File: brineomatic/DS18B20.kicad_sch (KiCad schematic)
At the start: 4 parts

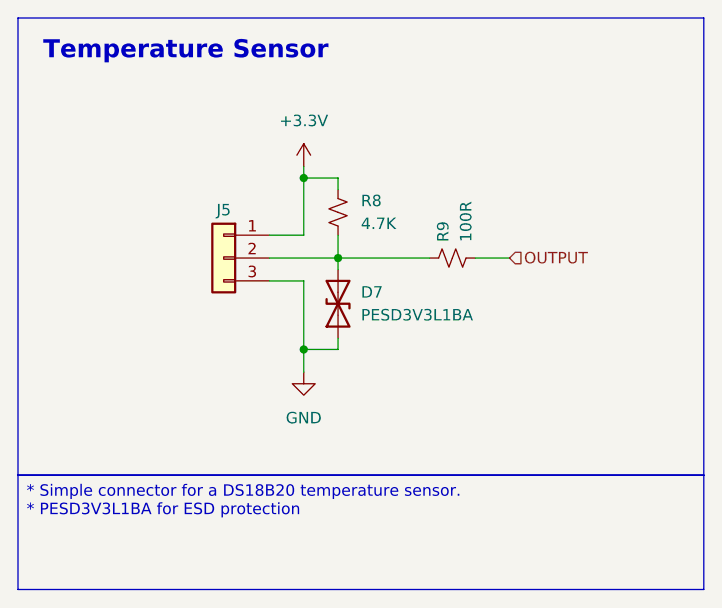
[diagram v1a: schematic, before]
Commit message: cleaned up hierarchical pin settings
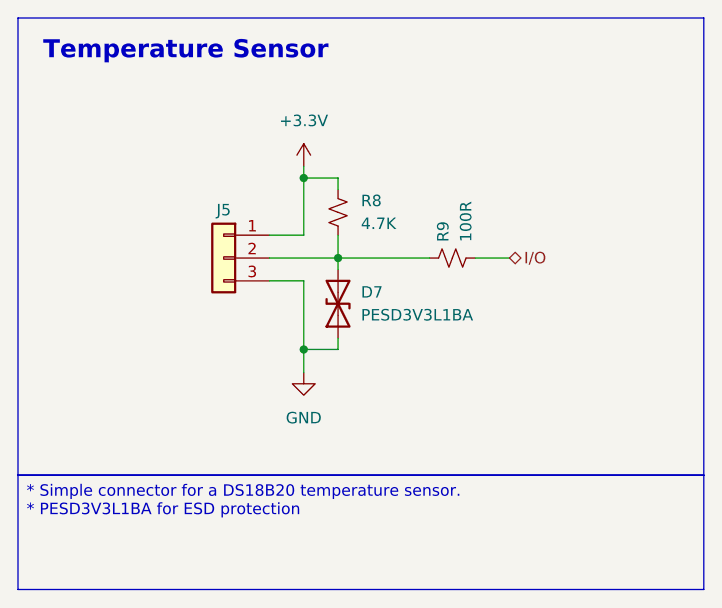
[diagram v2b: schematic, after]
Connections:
- net OUTPUT renamed I/O
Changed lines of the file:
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@@
 		)
 	)
-	(hierarchical_label "OUTPUT"
-		(shape input)
+	(hierarchical_label "I{slash}O"
+		(shape bidirectional)
 		(at 142.24 93.98 0)
 		(effects

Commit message: holy re-routing batman. board is fully routed first pass.
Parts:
- added C4: 1uF, Capacitor_SMD:C_0603_1608Metric, symbol Device:C_Small
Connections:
- net +3.3V: now also C4.1
- net GND: now also C4.2
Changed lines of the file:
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@@
+	(wire
+		(pts
+			(xy 119.38 104.14) (xy 97.79 104.14)
+		)
+		(stroke
+			(width 0)
+			(type default)
+		)
+	)
 	(wire
 		(pts
@@
 	(wire
 		(pts
+			(xy 119.38 85.09) (xy 97.79 85.09)
+		)
+		(stroke
+			(width 0)
+			(type default)
+		)
+	)
+	(wire
+		(pts
 			(xy 119.38 104.14) (xy 119.38 106.68)
 		)
@@
 	(wire
 		(pts
+			(xy 97.79 85.09) (xy 97.79 91.44)
+		)
+		(stroke
+			(width 0)
+			(type default)
+		)
+	)
+	(wire
+		(pts
 			(xy 123.19 91.44) (xy 123.19 93.98)
 		)
@@
 		(pts
 			(xy 123.19 104.14) (xy 123.19 102.87)
+		)
+		(stroke
+			(width 0)
+			(type default)
+		)
+	)
+	(wire
+		(pts
+			(xy 97.79 96.52) (xy 97.79 104.14)
 		)
 		(stroke
@@
 			)
 			(justify left)
+		)
+	)
+	(symbol
+		(lib_id "Device:C_Small")
+		(at 97.79 93.98 0)
+		(unit 1)
+		(exclude_from_sim no)
+		(in_bom yes)
+		(on_board yes)
+		(dnp no)
+		(fields_autoplaced yes)
+		(property "Reference" "C4"
+			(at 100.33 92.7162 0)
+			(effects
+				(font
+					(size 1.27 1.27)
+				)
+				(justify left)
+			)
+		)
+		(property "Value" "1uF"
+			(at 100.33 95.2562 0)
+			(effects
+				(font
+					(size 1.27 1.27)
+				)
+				(justify left)
+			)
+		)
+		(property "Footprint" "Capacitor_SMD:C_0603_1608Metric"
+			(at 97.79 93.98 0)
+			(effects
+				(font
+					(size 1.27 1.27)
+				)
+				(hide yes)
+			)
+		)
+		(property "Datasheet" "~"
+			(at 97.79 93.98 0)
+			(effects
+				(font
+					(size 1.27 1.27)
+				)
+				(hide yes)
+			)
+		)
+		(property "Description" ""
+			(at 97.79 93.98 0)
+			(effects
+				(font
+					(size 1.27 1.27)
+				)
+			)
+		)
+		(property "LCSC Part Name" ""
+			(at 97.79 93.98 0)
+			(effects
+				(font
+					(size 1.27 1.27)
+				)
+				(hide yes)
+			)
+		)
+		(property "Manufacturer" ""
+			(at 97.79 93.98 0)
+			(effects
+				(font
+					(size 1.27 1.27)
+				)
+				(hide yes)
+			)
+		)
+		(property "Manufacturer Part" ""
+			(at 97.79 93.98 0)
+			(effects
+				(font
+					(size 1.27 1.27)
+				)
+				(hide yes)
+			)
+		)
+		(property "Supplier" ""
+			(at 97.79 93.98 0)
+			(effects
+				(font
+					(size 1.27 1.27)
+				)
+				(hide yes)
+			)
+		)
+		(property "Supplier Part" ""
+			(at 97.79 93.98 0)
+			(effects
+				(font
+					(size 1.27 1.27)
+				)
+				(hide yes)
+			)
+		)
+		(pin "1"
+		)
+		(pin "2"
+		)
+		(instances
+			(project "brineomatic"
+				(path "/96477ae2-ef08-48f3-8dd4-fe4478541f68/4c28a3dc-9363-4fde-b010-be952dc8ce44"
+					(reference "C58")
+					(unit 1)
+				)
+				(path "/96477ae2-ef08-48f3-8dd4-fe4478541f68/7dc38cc9-02c6-4108-8c2f-d0f758210cae"
+					(reference "C4")
+					(unit 1)
+				)
+			)
 		)
 	)
@@
 			(project "brineomatic"
 				(path "/96477ae2-ef08-48f3-8dd4-fe4478541f68/4c28a3dc-9363-4fde-b010-be952dc8ce44"
-					(reference "D44")
+					(reference "D43")
 					(unit 1)
 				)

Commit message: added test points
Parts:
- added TP4: TestPoint, TestPoint:TestPoint_Pad_D1.5mm, symbol Connector:TestPoint
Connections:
- net at D7.2 (A2), J5.2 (Pin_2), R8.1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: now also TP4.1
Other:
- moved on the sheet: D7, R8, R9
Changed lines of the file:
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@@
+	)
+	(junction
+		(at 124.46 93.98)
+		(diameter 0)
+		(color 0 0 0 0)
 	)
 	(junction
@@
 	)
 	(junction
-		(at 123.19 93.98)
+		(at 132.08 93.98)
 		(diameter 0)
 		(color 0 0 0 0)
@@
 	(wire
 		(pts
-			(xy 123.19 93.98) (xy 133.35 93.98)
+			(xy 132.08 93.98) (xy 142.24 93.98)
 		)
 		(stroke
@@
 	(wire
 		(pts
-			(xy 123.19 85.09) (xy 123.19 86.36)
+			(xy 132.08 85.09) (xy 132.08 86.36)
 		)
 		(stroke
@@
 	(wire
 		(pts
-			(xy 119.38 104.14) (xy 123.19 104.14)
-		)
-		(stroke
-			(width 0)
-			(type default)
-		)
-	)
-	(wire
-		(pts
-			(xy 119.38 85.09) (xy 123.19 85.09)
-		)
-		(stroke
-			(width 0)
-			(type default)
-		)
-	)
-	(wire
-		(pts
-			(xy 115.57 93.98) (xy 123.19 93.98)
+			(xy 119.38 104.14) (xy 132.08 104.14)
+		)
+		(stroke
+			(width 0)
+			(type default)
+		)
+	)
+	(wire
+		(pts
+			(xy 119.38 85.09) (xy 132.08 85.09)
+		)
+		(stroke
+			(width 0)
+			(type default)
+		)
+	)
+	(wire
+		(pts
+			(xy 115.57 93.98) (xy 124.46 93.98)
 		)
 		(stroke
@@
 	(wire
 		(pts
-			(xy 123.19 91.44) (xy 123.19 93.98)
+			(xy 132.08 91.44) (xy 132.08 93.98)
 		)
 		(stroke
@@
 	(wire
 		(pts
-			(xy 138.43 93.98) (xy 142.24 93.98)
-		)
-		(stroke
-			(width 0)
-			(type default)
-		)
-	)
-	(wire
-		(pts
-			(xy 123.19 95.25) (xy 123.19 93.98)
+			(xy 124.46 93.98) (xy 132.08 93.98)
+		)
+		(stroke
+			(width 0)
+			(type default)
+		)
+	)
+	(wire
+		(pts
+			(xy 147.32 93.98) (xy 151.13 93.98)
+		)
+		(stroke
+			(width 0)
+			(type default)
+		)
+	)
+	(wire
+		(pts
+			(xy 132.08 95.25) (xy 132.08 93.98)
 		)
 		(stroke
@@
 	(wire
 		(pts
-			(xy 123.19 104.14) (xy 123.19 102.87)
+			(xy 132.08 104.14) (xy 132.08 102.87)
 		)
 		(stroke
@@
 	(hierarchical_label "I{slash}O"
 		(shape bidirectional)
-		(at 142.24 93.98 0)
+		(at 151.13 93.98 0)
 		(effects
 			(font
@@
 	(symbol
 		(lib_id "Device:D_TVS")
-		(at 123.19 99.06 90)
+		(at 132.08 99.06 90)
 		(unit 1)
 		(exclude_from_sim no)
@@
 		(dnp no)
 		(property "Reference" "D7"
-			(at 125.73 97.7899 90)
+			(at 134.62 97.7899 90)
 			(effects
 				(font
@@
 		)
 		(property "Value" "PESD3V3L1BA"
-			(at 125.73 100.3299 90)
+			(at 134.62 100.3299 90)
 			(effects
 				(font
@@
 		)
 		(property "Footprint" "Diode_SMD:D_SOD-323"
-			(at 123.19 99.06 0)
+			(at 132.08 99.06 0)
 			(effects
 				(font
@@
 		)
 		(property "Datasheet" "~"
-			(at 123.19 99.06 0)
+			(at 132.08 99.06 0)
 			(effects
 				(font
@@
 		)
 		(property "Description" "Bidirectional transient-voltage-suppression diode"
-			(at 123.19 99.06 0)
+			(at 132.08 99.06 0)
 			(effects
 				(font
@@
 		)
 		(property "LCSC Part Name" ""
-			(at 123.19 99.06 90)
+			(at 132.08 99.06 90)
 			(effects
 				(font
@@
 		)
 		(property "Manufacturer" ""
-			(at 123.19 99.06 90)
+			(at 132.08 99.06 90)
 			(effects
 				(font
@@
 		)
 		(property "Manufacturer Part" ""
-			(at 123.19 99.06 90)
+			(at 132.08 99.06 90)
 			(effects
 				(font
@@
 		)
 		(property "Supplier" ""
-			(at 123.19 99.06 90)
+			(at 132.08 99.06 90)
 			(effects
 				(font
@@
 		)
 		(property "Supplier Part" ""
-			(at 123.19 99.06 90)
+			(at 132.08 99.06 90)
 			(effects
 				(font
@@
 		)
 		(property "LCSC" "C2687129"
-			(at 123.19 99.06 90)
+			(at 132.08 99.06 90)
 			(effects
 				(font
@@
 	)
 	(symbol
+		(lib_id "Connector:TestPoint")
+		(at 124.46 93.98 0)
+		(unit 1)
+		(exclude_from_sim no)
+		(in_bom yes)
+		(on_board yes)
+		(dnp no)
+		(property "Reference" "TP4"
+			(at 123.19 88.9 0)
+			(effects
+				(font
+					(size 1.27 1.27)
+				)
+				(justify left)
+			)
+		)
+		(property "Value" "TestPoint"
+			(at 127 91.9479 0)
+			(effects
+				(font
+					(size 1.27 1.27)
+				)
+				(justify left)
+				(hide yes)
+			)
+		)
+		(property "Footprint" "TestPoint:TestPoint_Pad_D1.5mm"
+			(at 129.54 93.98 0)
+			(effects
+				(font
+					(size 1.27 1.27)
+				)
+				(hide yes)
+			)
+		)
+		(property "Datasheet" "~"
+			(at 129.54 93.98 0)
+			(effects
+				(font
+					(size 1.27 1.27)
+				)
+				(hide yes)
+			)
+		)
+		(property "Description" "test point"
+			(at 124.46 93.98 0)
+			(effects
+				(font
+					(size 1.27 1.27)
+				)
+				(hide yes)
+			)
+		)
+		(pin "1"
+		)
+		(instances
+			(project "brineomatic"
+				(path "/96477ae2-ef08-48f3-8dd4-fe4478541f68/4c28a3dc-9363-4fde-b010-be952dc8ce44"
+					(reference "TP35")
+					(unit 1)
+				)
+				(path "/96477ae2-ef08-48f3-8dd4-fe4478541f68/7dc38cc9-02c6-4108-8c2f-d0f758210cae"
+					(reference "TP4")
+					(unit 1)
+				)
+			)
+		)
+	)
+	(symbol
 		(lib_id "Device:R_Small_US")
-		(at 135.89 93.98 270)
+		(at 144.78 93.98 270)
 		(unit 1)
 		(exclude_from_sim no)
@@
 		(dnp no)
 		(property "Reference" "R9"
-			(at 134.874 92.202 0)
+			(at 143.764 92.202 0)
 			(effects
 				(font
@@
 		)
 		(property "Value" "100R"
-			(at 137.414 92.202 0)
+			(at 146.304 92.202 0)
 			(effects
 				(font
@@
 		)
 		(property "Footprint" "Resistor_SMD:R_0603_1608Metric"
-			(at 135.89 93.98 0)
+			(at 144.78 93.98 0)
 			(effects
 				(font
@@
 		)
 		(property "Datasheet" "~"
-			(at 135.89 93.98 0)
+			(at 144.78 93.98 0)
 			(effects
 				(font
@@
 		)
 		(property "Description" "Resistor, small US symbol"
-			(at 135.89 93.98 0)
+			(at 144.78 93.98 0)
 			(effects
 				(font
@@
 		)
 		(property "LCSC" ""
-			(at 135.89 93.98 0)
+			(at 144.78 93.98 0)
 			(effects
 				(font
@@
 	(symbol
 		(lib_id "Device:R_Small_US")
-		(at 123.19 88.9 180)
+		(at 132.08 88.9 180)
 		(unit 1)
 		(exclude_from_sim no)
@@
 		(fields_autoplaced yes)
 		(property "Reference" "R8"
-			(at 125.73 87.6299 0)
+			(at 134.62 87.6299 0)
 			(effects
 				(font
@@
 		)
 		(property "Value" "4.7K"
-			(at 125.73 90.1699 0)
+			(at 134.62 90.1699 0)
 			(effects
 				(font
@@
 		)
 		(property "Footprint" "Resistor_SMD:R_0603_1608Metric"
-			(at 123.19 88.9 0)
+			(at 132.08 88.9 0)
 			(effects
 				(font
@@
 		)
 		(property "Datasheet" "~"
-			(at 123.19 88.9 0)
+			(at 132.08 88.9 0)
 			(effects
 				(font
@@
 		)
 		(property "Description" "Resistor, small US symbol"
-			(at 123.19 88.9 0)
+			(at 132.08 88.9 0)
 			(effects
 				(font
@@
 		)
 		(property "LCSC" " C23162"
-			(at 123.19 88.9 0)
-			(effects
-				(font
+			(at 132.08 88.9 0)
+			(effects
+				(font

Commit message: bom and placement verified
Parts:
- C4: LCSC (none) -> C15849
- R9: LCSC (none) -> C22775
- TP4: now left out of the parts list
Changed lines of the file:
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@@
+			)
+		)
+		(property "LCSC" "C15849"
+			(at 97.79 93.98 0)
+			(effects
+				(font
+					(size 1.27 1.27)
+				)
+				(hide yes)
 			)
 		)
@@
 		(unit 1)
 		(exclude_from_sim no)
-		(in_bom yes)
+		(in_bom no)
 		(on_board yes)
 		(dnp no)
@@
 			)
 		)
-		(property "LCSC" ""
+		(property "LCSC" "C22775"
 			(at 144.78 93.98 0)
 			(effects

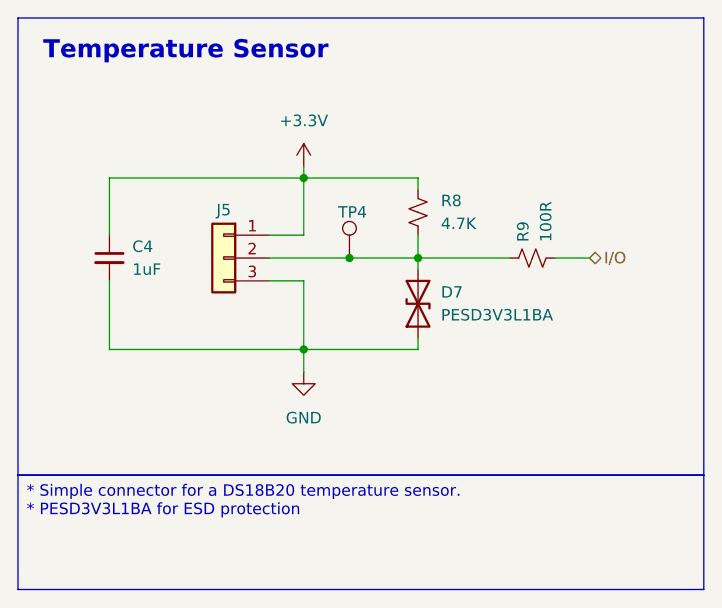
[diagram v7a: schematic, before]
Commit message: Updating schematic for Rev D: * Original ADS1115   * brine tds (same)   * product tds (same)   * bus voltage (new)   * spare 4-20ma sensor (new)
* Add 2nd ADS1115 -> only 4-20ma sensors
  * pre-filter pressure - jst 2.0
  * mid-filter pressure - jst 2.0
  * post-filter pressure - jst 2.0
  * high pressure - jst 2.0
  * alert pin -> gpio3
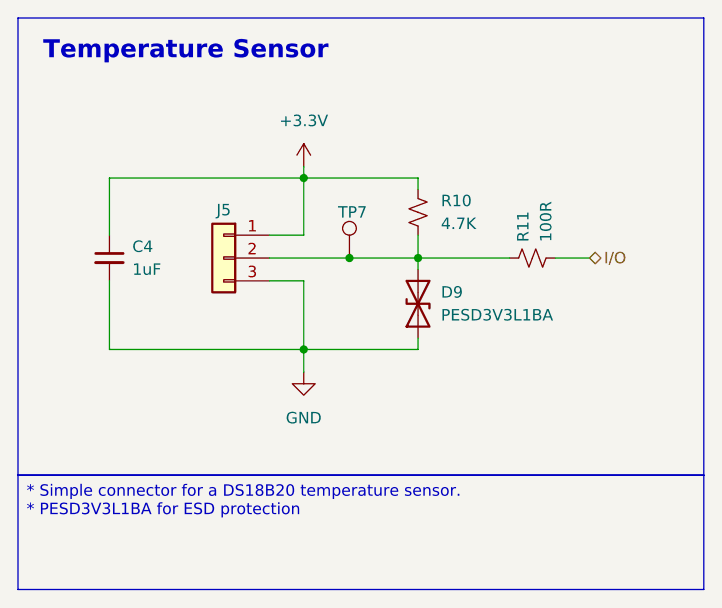
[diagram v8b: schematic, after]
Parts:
- renumbered D7 to D9, R8 to R10, R9 to R11, TP4 to TP7
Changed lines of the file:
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@@
 	(title_block
 		(title "https://github.com/hoeken/brineomatic")
-		(date "2026-01-08")
-		(rev "C1")
+		(date "2026-06-02")
+		(rev "D")
 	)
 	(rectangle
@@
 			(project "brineomatic"
 				(path "/96477ae2-ef08-48f3-8dd4-fe4478541f68/4c28a3dc-9363-4fde-b010-be952dc8ce44"
-					(reference "C58")
+					(reference "C57")
 					(unit 1)
 				)
@@
 		(on_board yes)
 		(dnp no)
-		(property "Reference" "D7"
+		(property "Reference" "D9"
 			(at 134.62 97.7899 90)
 			(effects
@@
 			(project "brineomatic"
 				(path "/96477ae2-ef08-48f3-8dd4-fe4478541f68/4c28a3dc-9363-4fde-b010-be952dc8ce44"
-					(reference "D43")
+					(reference "D50")
 					(unit 1)
 				)
 				(path "/96477ae2-ef08-48f3-8dd4-fe4478541f68/7dc38cc9-02c6-4108-8c2f-d0f758210cae"
-					(reference "D7")
+					(reference "D9")
 					(unit 1)
 				)
@@
 		(dnp no)
 		(fields_autoplaced yes)
-		(property "Reference" "#PWR019"
+		(property "Reference" "#PWR022"
 			(at 119.38 113.03 0)
 			(effects
@@
 			(project "brineomatic"
 				(path "/96477ae2-ef08-48f3-8dd4-fe4478541f68/4c28a3dc-9363-4fde-b010-be952dc8ce44"
-					(reference "#PWR069")
+					(reference "#PWR073")
 					(unit 1)
 				)
 				(path "/96477ae2-ef08-48f3-8dd4-fe4478541f68/7dc38cc9-02c6-4108-8c2f-d0f758210cae"
-					(reference "#PWR019")
+					(reference "#PWR022")
 					(unit 1)
 				)
@@
 		(on_board yes)
 		(dnp no)
-		(property "Reference" "TP4"
+		(property "Reference" "TP7"
 			(at 123.19 88.9 0)
 			(effects
@@
 			(project "brineomatic"
 				(path "/96477ae2-ef08-48f3-8dd4-fe4478541f68/4c28a3dc-9363-4fde-b010-be952dc8ce44"
-					(reference "TP35")
+					(reference "TP41")
 					(unit 1)
 				)
 				(path "/96477ae2-ef08-48f3-8dd4-fe4478541f68/7dc38cc9-02c6-4108-8c2f-d0f758210cae"
-					(reference "TP4")
+					(reference "TP7")
 					(unit 1)
 				)
@@
 		(on_board yes)
 		(dnp no)
-		(property "Reference" "R9"
+		(property "Reference" "R11"
 			(at 143.764 92.202 0)
 			(effects
@@
 			(project "brineomatic"
 				(path "/96477ae2-ef08-48f3-8dd4-fe4478541f68/4c28a3dc-9363-4fde-b010-be952dc8ce44"
-					(reference "R62")
+					(reference "R68")
 					(unit 1)
 				)
 				(path "/96477ae2-ef08-48f3-8dd4-fe4478541f68/7dc38cc9-02c6-4108-8c2f-d0f758210cae"
-					(reference "R9")
+					(reference "R11")
 					(unit 1)
 				)
@@
 		(dnp no)
 		(fields_autoplaced yes)
-		(property "Reference" "R8"
+		(property "Reference" "R10"
 			(at 134.62 87.6299 0)
 			(effects
@@
 			(project "brineomatic"
 				(path "/96477ae2-ef08-48f3-8dd4-fe4478541f68/4c28a3dc-9363-4fde-b010-be952dc8ce44"
-					(reference "R61")
+					(reference "R67")
 					(unit 1)
 				)
 				(path "/96477ae2-ef08-48f3-8dd4-fe4478541f68/7dc38cc9-02c6-4108-8c2f-d0f758210cae"
-					(reference "R8")
+					(reference "R10")
 					(unit 1)
 				)
@@
 		(dnp no)
 		(fields_autoplaced yes)
-		(property "Reference" "#PWR018"
+		(property "Reference" "#PWR021"
 			(at 119.38 87.63 0)
 			(effects
@@
 			(project "brineomatic"
 				(path "/96477ae2-ef08-48f3-8dd4-fe4478541f68/4c28a3dc-9363-4fde-b010-be952dc8ce44"
-					(reference "#PWR068")
+					(reference "#PWR072")
 					(unit 1)
 				)
 				(path "/96477ae2-ef08-48f3-8dd4-fe4478541f68/7dc38cc9-02c6-4108-8c2f-d0f758210cae"
-					(reference "#PWR018")
-					(unit 1)
-				)
+					(reference "#PWR021")
+					(unit 1)
+				)
